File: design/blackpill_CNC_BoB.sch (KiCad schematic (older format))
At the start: 183 parts, among them J13 VMOT, J14 Spindle/Coolant, J15 Control, J17 UART, J18 Limits, J19 GPIO, J20 Power out, J23 Reset, J25 UART1, U10 74LVC2G17, U2 TLP290-4, U3 TLP290-4, U8 TLP290-4

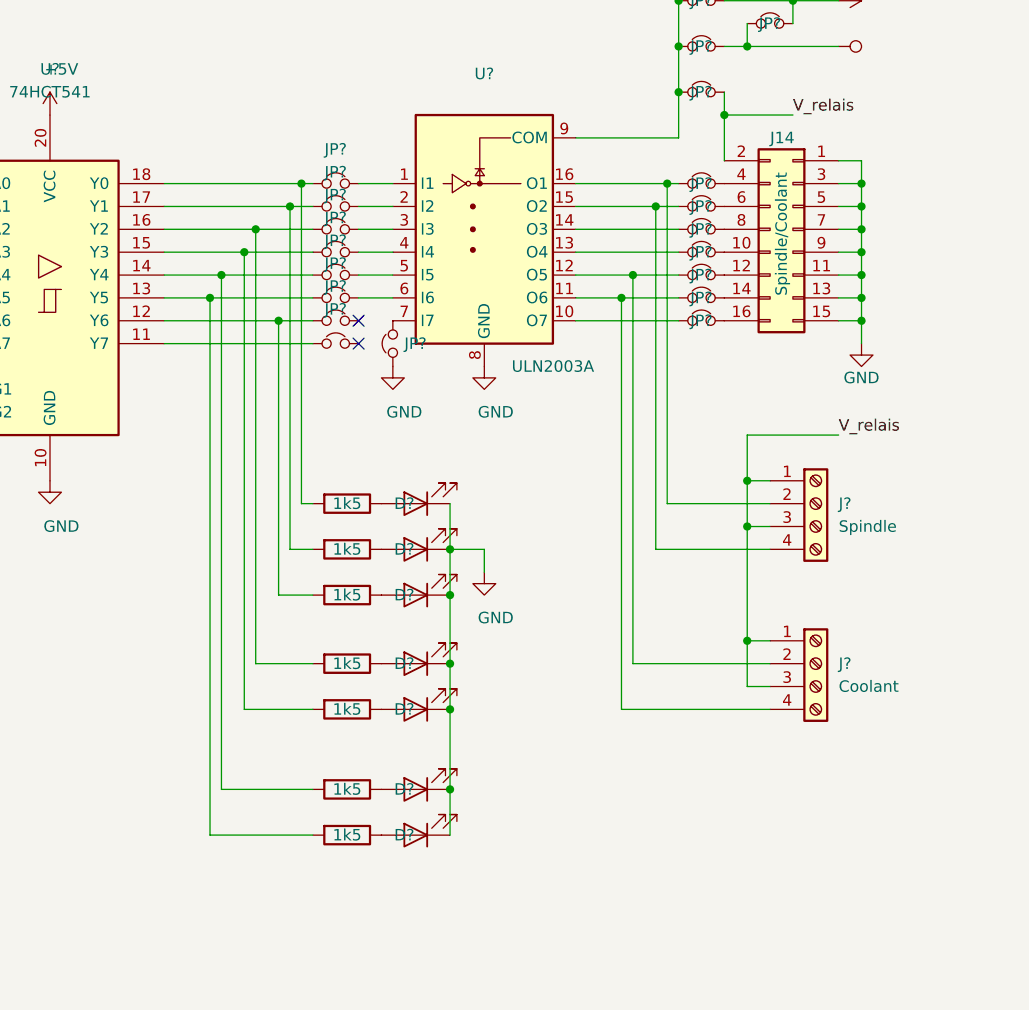
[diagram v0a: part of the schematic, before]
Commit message: labelling out driver for transparency
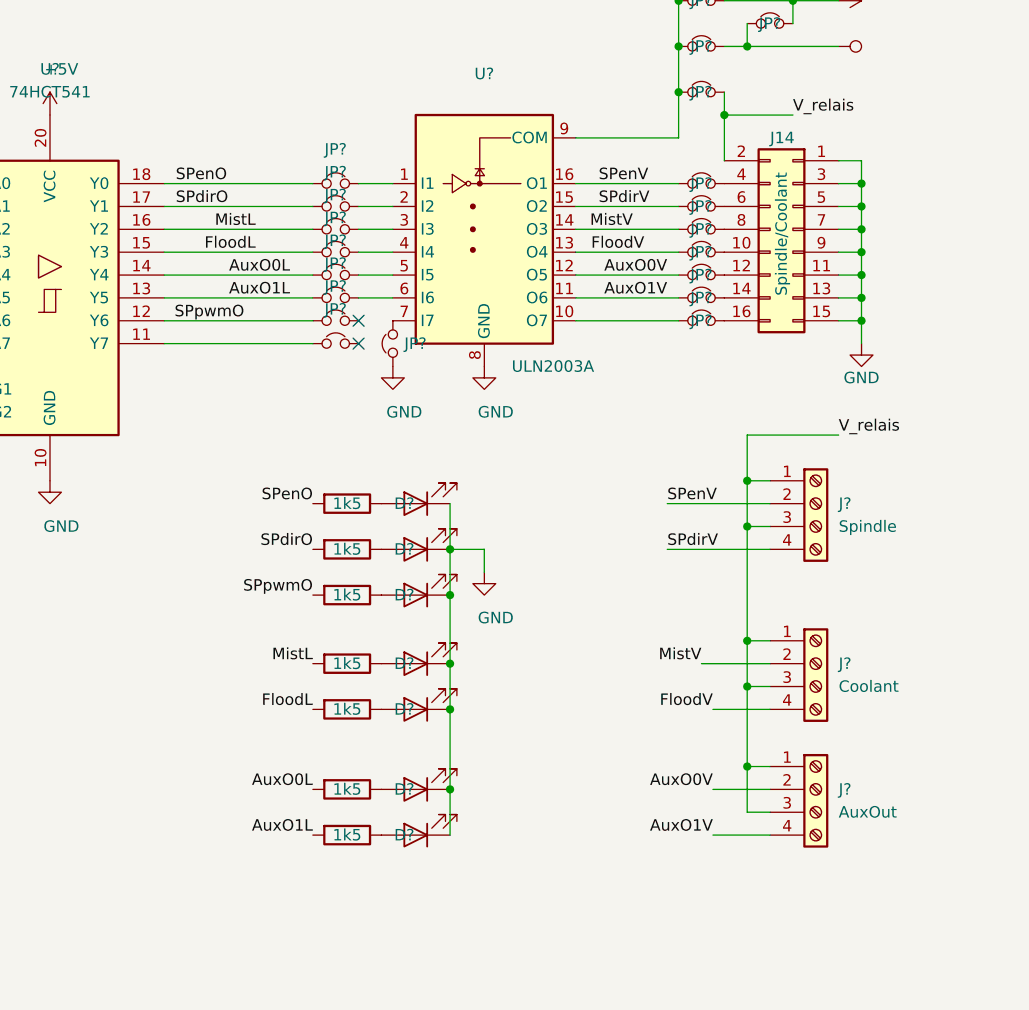
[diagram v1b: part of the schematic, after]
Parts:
- added J?: AuxOut, symbol Connector:Screw_Terminal_01x04
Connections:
- net labels added: AuxO0L, AuxO0V, AuxO1L, AuxO1V, FloodL, FloodV, MistL, MistV, SPdirO, SPdirV, SPenO, SPenV, SPpwmO
- wire segments 489 -> 466
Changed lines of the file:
@@
 	1    0    0    -1
 $EndComp
-Wire Wire Line
-	14250 6700 14600 6700
 $Comp
 L Device:Jumper_NC_Small JP?
@@
 	1    0    0    -1
 $EndComp
-Wire Wire Line
-	14250 6600 14650 6600
 $Comp
 L Device:Jumper_NC_Small JP?
@@
 	1    0    0    -1
 $EndComp
-Wire Wire Line
-	14250 7000 14500 7000
 $Comp
 L Device:Jumper_NC_Small JP?
@@
 	1    0    0    -1
 $EndComp
-Wire Wire Line
-	14250 7100 14450 7100
 $Comp
 L Device:Jumper_NC_Small JP?
@@
 	1    0    0    -1
 $EndComp
-Wire Wire Line
-	14250 7200 14700 7200
 $Comp
 L Nucleo64-CNC-rescue:Vdrive-power #PWR?
@@
 Wire Wire Line
 	15100 8000 14650 8000
-Wire Wire Line
-	14650 8000 14650 6600
-Connection ~ 14650 6600
-Wire Wire Line
-	14650 6600 14700 6600
-Wire Wire Line
-	14600 6700 14600 8200
-Wire Wire Line
-	14600 8200 15100 8200
-Connection ~ 14600 6700
-Wire Wire Line
-	14600 6700 14700 6700
-Wire Wire Line
-	14500 7000 14500 8700
-Wire Wire Line
-	14500 8700 15100 8700
-Wire Wire Line
-	14450 7100 14450 8900
-Wire Wire Line
-	14450 8900 15100 8900
 $Comp
 L Device:R R?
@@
 Connection ~ 13700 8200
 Wire Wire Line
-	12450 6600 13050 6600
-Wire Wire Line
-	12450 6700 13000 6700
-Wire Wire Line
-	12450 6800 12850 6800
-Wire Wire Line
-	12450 6900 12800 6900
-Wire Wire Line
-	12450 7000 12700 7000
-Wire Wire Line
-	12450 7100 12650 7100
-Wire Wire Line
-	12450 7200 12950 7200
-Wire Wire Line
 	12450 7300 13100 7300
 $Comp
@@
 	-1   0    0    1
 $EndComp
-Connection ~ 14450 7100
-Wire Wire Line
-	14450 7100 14700 7100
-Connection ~ 14500 7000
-Wire Wire Line
-	14500 7000 14700 7000
-Wire Wire Line
-	14250 6800 14700 6800
-Wire Wire Line
-	14250 6900 14700 6900
 Wire Wire Line
 	15000 8100 15000 8600
@@
 	13700 8900 13700 9250
 Connection ~ 13700 8900
-Wire Wire Line
-	13100 8000 13050 8000
-Wire Wire Line
-	13050 8000 13050 6600
-Wire Wire Line
-	13050 6600 13100 6600
-Wire Wire Line
-	13000 6700 13000 8200
-Wire Wire Line
-	13000 8200 13100 8200
-Wire Wire Line
-	13000 6700 13100 6700
-Wire Wire Line
-	12950 7200 12950 8400
-Wire Wire Line
-	12950 8400 13100 8400
-Wire Wire Line
-	12950 7200 13100 7200
-Wire Wire Line
-	13100 8700 12850 8700
-Wire Wire Line
-	12850 8700 12850 6800
-Wire Wire Line
-	12850 6800 13100 6800
-Wire Wire Line
-	12800 6900 12800 8900
-Wire Wire Line
-	12800 8900 13100 8900
-Connection ~ 12800 6900
-Wire Wire Line
-	12800 6900 13100 6900
-Wire Wire Line
-	12700 7000 12700 9250
-Wire Wire Line
-	12700 9250 13100 9250
-Connection ~ 12700 7000
-Wire Wire Line
-	12700 7000 13100 7000
-Wire Wire Line
-	12650 9450 13100 9450
-Connection ~ 12850 6800
-Connection ~ 12950 7200
-Connection ~ 13000 6700
-Connection ~ 13050 6600
 Wire Wire Line
 	11450 7600 11450 7750
@@
 	1    0    0    -1
 $EndComp
-Wire Wire Line
-	12650 7100 12650 9450
-Connection ~ 12650 7100
-Wire Wire Line
-	12650 7100 13100 7100
 $Comp
 L Connector_Generic:Conn_01x04 J?
@@
 Text Label 9400 1200 2    50   ~ 0
 ~Strobe
+Text Label 14650 8000 0    50   ~ 0
+SPenV
+Text Label 14650 8200 0    50   ~ 0
+SPdirV
+Text Label 12500 6600 0    50   ~ 0
+SPenO
+Text Label 12500 6700 0    50   ~ 0
+SPdirO
+Text Label 13100 8400 2    50   ~ 0
+SPpwmO
+Text Label 14800 8700 2    50   ~ 0
+MistV
+Text Label 14850 8900 2    50   ~ 0
+FloodV
+$Comp
+L Connector:Screw_Terminal_01x04 J?
+U 1 1 6FBF74D8
+P 15300 9250
+F 0 "J?" H 15400 9250 50  0000 L CNN
+F 1 "AuxOut" H 15400 9150 50  0000 L CNN
+F 2 "" H 15300 9250 50  0001 C CNN
+F 3 "~" H 15300 9250 50  0001 C CNN
+	1    15300 9250
+	1    0    0    -1
+$EndComp
+Wire Wire Line
+	14250 7200 14700 7200
+Wire Wire Line
+	15100 9350 15000 9350
+Wire Wire Line
+	15000 9350 15000 9150
+Connection ~ 15000 8800
+Wire Wire Line
+	15100 9150 15000 9150
+Connection ~ 15000 9150
+Wire Wire Line
+	15000 9150 15000 8800
+Text Label 14850 9250 2    50   ~ 0
+AuxO0V
+Text Label 14850 9450 2    50   ~ 0
+AuxO1V
+Text Label 13100 8700 2    50   ~ 0
+MistL
+Text Label 13100 8900 2    50   ~ 0
+FloodL
+Text Label 13100 9250 2    50   ~ 0
+AuxO0L
+Text Label 13100 9450 2    50   ~ 0
+AuxO1L
+Wire Wire Line
+	12450 6600 13100 6600
+Wire Wire Line
+	12450 6700 13100 6700
+Wire Wire Line
+	12450 7200 13100 7200
+Wire Wire Line
+	12450 6800 13100 6800
+Wire Wire Line
+	12450 6900 13100 6900
+Wire Wire Line
+	12450 7000 13100 7000
+Wire Wire Line
+	12450 7100 13100 7100
+Text Label 12800 7200 2    50   ~ 0
+SPpwmO
+Text Label 13100 8000 2    50   ~ 0
+SPenO
+Text Label 13100 8200 2    50   ~ 0
+SPdirO
+Text Label 12850 6800 2    50   ~ 0
+MistL
+Text Label 12850 6900 2    50   ~ 0
+FloodL
+Text Label 13000 7000 2    50   ~ 0
+AuxO0L
+Text Label 13000 7100 2    50   ~ 0
+AuxO1L
+Wire Wire Line
+	14250 6600 14700 6600
+Wire Wire Line
+	14250 6700 14700 6700
+Wire Wire Line
+	14250 6800 14700 6800
+Wire Wire Line
+	14250 6900 14700 6900
+Wire Wire Line
+	14250 7100 14700 7100
+Wire Wire Line
+	14250 7000 14700 7000
+Text Label 14350 6600 0    50   ~ 0
+SPenV
+Text Label 14350 6700 0    50   ~ 0
+SPdirV
+Text Label 14500 6800 2    50   ~ 0
+MistV
+Text Label 14550 6900 2    50   ~ 0
+FloodV
+Text Label 14650 7000 2    50   ~ 0
+AuxO0V
+Text Label 14650 7100 2    50   ~ 0
+AuxO1V
+Wire Wire Line
+	14650 8200 15100 8200
+Wire Wire Line
+	14800 8700 15100 8700
+Wire Wire Line
+	14850 8900 15100 8900
+Wire Wire Line
+	14850 9250 15100 9250
+Wire Wire Line
+	14850 9450 15100 9450
 $EndSCHEMATC

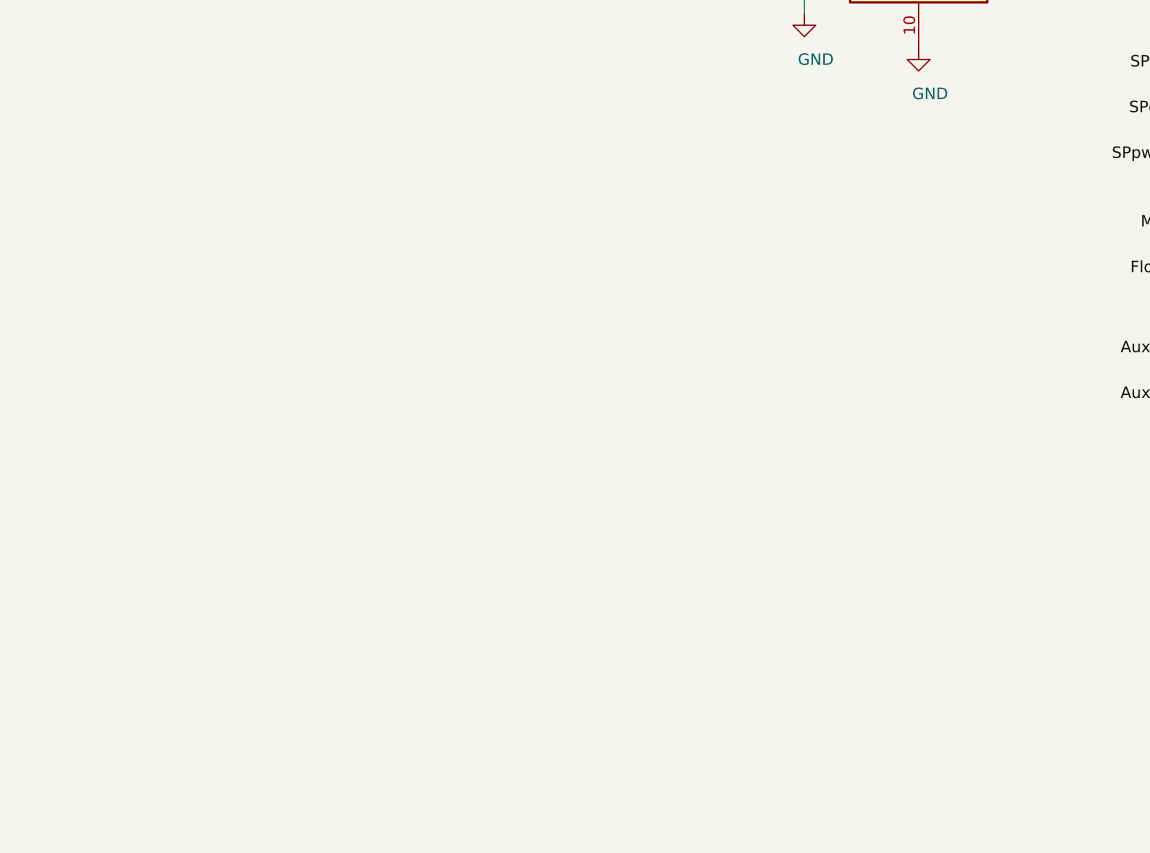
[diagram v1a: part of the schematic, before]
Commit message: 10V-lowpass-Analog spindle PWM
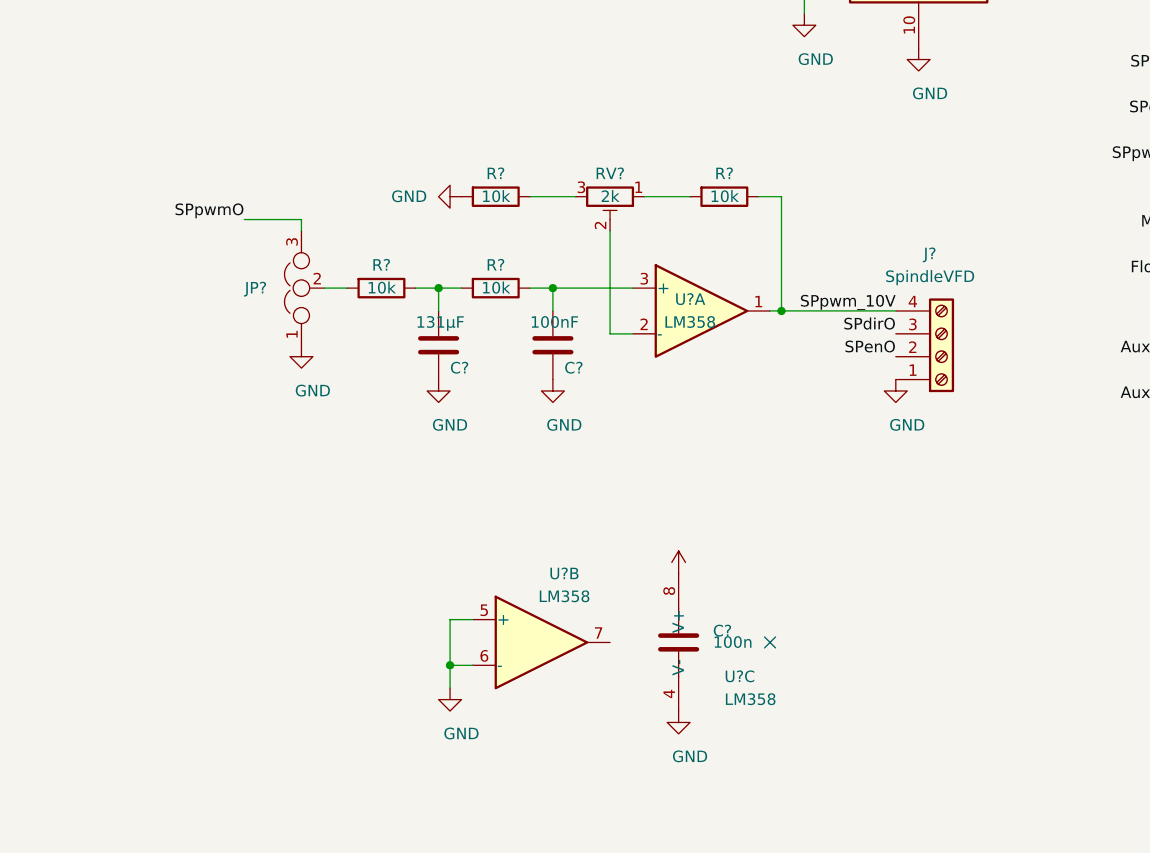
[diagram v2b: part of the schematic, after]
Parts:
- added C?: 131µF, symbol Device:C
- added C?: 100n, symbol Device:C
- added C?: 100nF, symbol Device:C
- added J?: SpindleVFD, symbol Connector:Screw_Terminal_01x04
- added JP?: Jumper_NC_Dual, symbol Device:Jumper_NC_Dual
- added R? (x4): 10k, symbol Device:R
- added RV?: 2k, symbol Device:R_POT_TRIM
- added U? (x3): LM358, symbol Amplifier_Operational:LM358
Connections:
- net labels added: SPpwm_10V
- wire segments 466 -> 487
- no-connect marks 11 -> 12

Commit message: reaarange input OC stuff
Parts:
- removed J15: Control, symbol Connector_Generic:Conn_02x05_Odd_Even
- removed J17: UART, symbol Connector_Generic:Conn_01x03
- removed J18: Limits, symbol Connector_Generic:Conn_02x04_Odd_Even
- removed J25: UART1, symbol Connector_Generic:Conn_01x03
- removed R1, R24, R4, R40, R6, R8: 470, symbol Device:R
- added J?: UART1, symbol Connector_Generic:Conn_01x04
- added J?: stepDriverLim, symbol Connector_Generic:Conn_01x06
- added J?: ALimIN, symbol Connector:Screw_Terminal_01x02
- added J?: ZLimIN, symbol Connector:Screw_Terminal_01x02
- added J?: YLimIN, symbol Connector:Screw_Terminal_01x02
- added J? (x2): XLimIN, symbol Connector:Screw_Terminal_01x02
- added J?: CS_IN, symbol Connector:Screw_Terminal_01x02
- added J?: FH_IN, symbol Connector:Screw_Terminal_01x02
- added J?: DoorIN, symbol Connector:Screw_Terminal_01x02
- added J?: ResetIN, symbol Connector:Screw_Terminal_01x02
- added J?: ProbeIN, symbol Connector:Screw_Terminal_01x02
- added R? (x7): 470, symbol Device:R
- C?: value 100n -> 100nF
- J19: value GPIO -> AuxEncIn
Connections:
- wire segments 487 -> 468
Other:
- moved on the sheet: C?, J19, J?, R10, R12, R14, R16, R2, R36, R41, R42, R43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

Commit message: 2 mA low current LED
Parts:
- removed J?: XLimIN, symbol Connector:Screw_Terminal_01x02
- removed R?: 470, symbol Device:R
- R? (x7): value 1k5 -> 2k
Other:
- moved on the sheet: J19, R42, R43, U10A, U10B
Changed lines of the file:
@@
 L Connector_Generic:Conn_01x04 J19
 U 1 1 5F98F511
-P 1000 8600
-F 0 "J19" H 1100 8300 50  0000 R CNN
-F 1 "AuxEncIn" V 1100 8650 50  0000 R CNN
-F 2 "" H 1000 8600 50  0001 C CNN
-F 3 "~" H 1000 8600 50  0001 C CNN
-	1    1000 8600
+P 1000 8300
+F 0 "J19" H 1100 8000 50  0000 R CNN
+F 1 "AuxEncIn" V 1100 8350 50  0000 R CNN
+F 2 "" H 1000 8300 50  0001 C CNN
+F 3 "~" H 1000 8300 50  0001 C CNN
+	1    1000 8300
 	-1   0    0    1
 $EndComp
@@
 L power:GND #PWR0128
 U 1 1 605D3E35
-P 1200 9400
-F 0 "#PWR0128" H 1200 9150 50  0001 C CNN
-F 1 "GND" H 1205 9227 50  0000 C CNN
-F 2 "" H 1200 9400 50  0001 C CNN
-F 3 "" H 1200 9400 50  0001 C CNN
-	1    1200 9400
+P 1200 9100
+F 0 "#PWR0128" H 1200 8850 50  0001 C CNN
+F 1 "GND" H 1205 8927 50  0000 C CNN
+F 2 "" H 1200 9100 50  0001 C CNN
+F 3 "" H 1200 9100 50  0001 C CNN
+	1    1200 9100
 	1    0    0    -1
 $EndComp
@@
 AuxIn1
 Wire Wire Line
-	1550 8500 1550 8300
-Text Label 2250 8850 0    50   ~ 0
+	1550 8200 1550 8000
+Text Label 2250 8550 0    50   ~ 0
 AuxIn0
 $Comp
 L Nucleo64-CNC-rescue:74LVC2G17-IoEngineering U10
 U 2 1 5FFBC3F7
-P 1900 8850
-F 0 "U10" H 1900 9142 40  0000 C CNN
-F 1 "74LVC2G17" H 1900 9066 40  0000 C CNN
-F 2 "" H 1995 8715 30  0001 C CNN
-F 3 "" H 2045 8965 60  0000 C CNN
-	2    1900 8850
+P 1900 8550
+F 0 "U10" H 1900 8842 40  0000 C CNN
+F 1 "74LVC2G17" H 1900 8766 40  0000 C CNN
+F 2 "" H 1995 8415 30  0001 C CNN
+F 3 "" H 2045 8665 60  0000 C CNN
+	2    1900 8550
 	1    0    0    -1
 $EndComp
-Text Label 2250 8300 0    50   ~ 0
+Text Label 2250 8000 0    50   ~ 0
 AuxIn1
 $Comp
 L Nucleo64-CNC-rescue:74LVC2G17-IoEngineering U10
 U 1 1 5FFBA6F5
-P 1900 8300
-F 0 "U10" H 1900 8652 40  0000 C CNN
-F 1 "74LVC2G17" H 1900 8576 40  0000 C CNN
-F 2 "" H 1900 8508 30  0001 C CNN
-F 3 "" H 2045 8415 60  0000 C CNN
-	1    1900 8300
+P 1900 8000
+F 0 "U10" H 1900 8352 40  0000 C CNN
+F 1 "74LVC2G17" H 1900 8276 40  0000 C CNN
+F 2 "" H 1900 8208 30  0001 C CNN
+F 3 "" H 2045 8115 60  0000 C CNN
+	1    1900 8000
 	1    0    0    -1
 $EndComp
 Wire Wire Line
-	1200 8500 1350 8500
+	1200 8200 1350 8200
 Text Label 4800 900  2    50   ~ 0
 ALim
@@
 L Device:R R43
 U 1 1 60CBF71A
-P 1550 9100
-F 0 "R43" H 1550 8950 50  0000 L CNN
-F 1 "10K" V 1550 9000 50  0000 L CNN
-F 2 "" V 1480 9100 50  0001 C CNN
-F 3 "~" H 1550 9100 50  0001 C CNN
-	1    1550 9100
+P 1550 8800
+F 0 "R43" H 1550 8650 50  0000 L CNN
+F 1 "10K" V 1550 8700 50  0000 L CNN
+F 2 "" V 1480 8800 50  0001 C CNN
+F 3 "~" H 1550 8800 50  0001 C CNN
+	1    1550 8800
 	1    0    0    -1
 $EndComp
 Wire Wire Line
-	1200 8600 1550 8600
+	1200 8300 1550 8300
 $Comp
 L Device:R R42
 U 1 1 60E403D9
-P 1350 9100
-F 0 "R42" H 1350 8950 50  0000 L CNN
-F 1 "10K" V 1350 9000 50  0000 L CNN
-F 2 "" V 1280 9100 50  0001 C CNN
-F 3 "~" H 1350 9100 50  0001 C CNN
-	1    1350 9100
+P 1350 8800
+F 0 "R42" H 1350 8650 50  0000 L CNN
+F 1 "10K" V 1350 8700 50  0000 L CNN
+F 2 "" V 1280 8800 50  0001 C CNN
+F 3 "~" H 1350 8800 50  0001 C CNN
+	1    1350 8800
 	1    0    0    -1
 $EndComp
 Wire Wire Line
-	1200 8700 1200 9350
+	1200 8400 1200 9050
 Wire Wire Line
-	1200 9350 1350 9350
+	1200 9050 1350 9050
 Wire Wire Line
-	1550 9350 1550 9250
-Connection ~ 1200 9350
+	1550 9050 1550 8950
+Connection ~ 1200 9050
 Wire Wire Line
-	1200 9350 1200 9400
+	1200 9050 1200 9100
 Wire Wire Line
-	1350 8950 1350 8500
-Connection ~ 1350 8500
+	1350 8650 1350 8200
+Connection ~ 1350 8200
 Wire Wire Line
-	1350 8500 1550 8500
+	1350 8200 1550 8200
 Wire Wire Line
-	1350 9250 1350 9350
-Connection ~ 1350 9350
+	1350 8950 1350 9050
+Connection ~ 1350 9050
 Wire Wire Line
-	1350 9350 1550 9350
+	1350 9050 1550 9050
 Wire Wire Line
 	2700 10850 2700 11000
 Wire Wire Line
-	1550 8600 1550 8850
+	1550 8300 1550 8550
 $Comp
 L YAAJ_WeAct_BlackPill_Part_Like:YAAJ_WeAct_BlackPill_Part_Like U?
@@
 P 13250 8000
 F 0 "R?" V 13000 8000 50  0001 C CNN
-F 1 "1k5" V 13250 8000 50  0000 C CNN
+F 1 "2k" V 13250 8000 50  0000 C CNN
 F 2 "" V 13180 8000 50  0001 C CNN
 F 3 "~" H 13250 8000 50  0001 C CNN
@@
 P 13250 8200
 F 0 "R?" V 13000 8200 50  0001 C CNN
-F 1 "1k5" V 13250 8200 50  0000 C CNN
+F 1 "2k" V 13250 8200 50  0000 C CNN
 F 2 "" V 13180 8200 50  0001 C CNN
 F 3 "~" H 13250 8200 50  0001 C CNN
@@
 P 13250 8700
 F 0 "R?" V 13000 8700 50  0001 C CNN
-F 1 "1k5" V 13250 8700 50  0000 C CNN
+F 1 "2k" V 13250 8700 50  0000 C CNN
 F 2 "" V 13180 8700 50  0001 C CNN
 F 3 "~" H 13250 8700 50  0001 C CNN
@@
 P 13250 8900
 F 0 "R?" V 13000 8900 50  0001 C CNN
-F 1 "1k5" V 13250 8900 50  0000 C CNN
+F 1 "2k" V 13250 8900 50  0000 C CNN
 F 2 "" V 13180 8900 50  0001 C CNN
 F 3 "~" H 13250 8900 50  0001 C CNN
@@
 P 13250 9250
 F 0 "R?" V 13000 9250 50  0001 C CNN
-F 1 "1k5" V 13250 9250 50  0000 C CNN
+F 1 "2k" V 13250 9250 50  0000 C CNN
 F 2 "" V 13180 9250 50  0001 C CNN
 F 3 "~" H 13250 9250 50  0001 C CNN
@@
 P 13250 9450
 F 0 "R?" V 13000 9450 50  0001 C CNN
-F 1 "1k5" V 13250 9450 50  0000 C CNN
+F 1 "2k" V 13250 9450 50  0000 C CNN
 F 2 "" V 13180 9450 50  0001 C CNN
 F 3 "~" H 13250 9450 50  0001 C CNN
@@
 P 13250 8400
 F 0 "R?" V 13000 8400 50  0001 C CNN
-F 1 "1k5" V 13250 8400 50  0000 C CNN
+F 1 "2k" V 13250 8400 50  0000 C CNN
 F 2 "" V 13180 8400 50  0001 C CNN
 F 3 "~" H 13250 8400 50  0001 C CNN
@@
 $Comp
 L Device:R R?
-U 1 1 7125B5DF
-P -600 3100
-F 0 "R?" H -600 2950 50  0000 L CNN
-F 1 "470" V -600 3000 50  0000 L CNN
-F 2 "" V -670 3100 50  0001 C CNN
-F 3 "~" H -600 3100 50  0001 C CNN
-	1    -600 3100
-	0    -1   -1   0
-$EndComp
-Wire Wire Line
-	-300 3100 -450 3100
-$Comp
-L Connector:Screw_Terminal_01x02 J?
-U 1 1 7125B5E7
-P -1150 3200
-F 0 "J?" H -1150 3000 50  0000 C CNN
-F 1 "XLimIN" V -1050 3150 50  0000 C CNN
-F 2 "" H -1150 3200 50  0001 C CNN
-F 3 "~" H -1150 3200 50  0001 C CNN
-	1    -1150 3200
-	-1   0    0    1
-$EndComp
-Wire Wire Line
-	-950 3200 -900 3200
-Wire Wire Line
-	-950 3100 -750 3100
-$Comp
-L Device:R R?
 U 1 1 7129471E
 P 1300 4300
@@
 	1000 6800 1000 6700
 Connection ~ 1000 6700
-Connection ~ 1550 8850
-Wire Wire Line
-	1550 8850 1550 8950
+Connection ~ 1550 8550
 Wire Wire Line
-	1200 8400 1200 7200
+	1550 8550 1550 8650
 Wire Wire Line
 	1200 7200 1250 7200
 Wire Wire Line
 	1550 7200 1600 7200
+Wire Wire Line
+	1200 8100 1200 7200
 $EndSCHEMATC
